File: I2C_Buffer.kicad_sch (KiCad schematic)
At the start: 6 parts, among them U2 LTC4300A-1IMS8_PBF

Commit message: BOM update
completed the BOM list
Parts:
- C19: MANUFACTURER (none) -> Murata Electronics; MANUFACTURER_PART_NUMBER (none) -> GCM155R71H103KA55J
- R11, R12, R3, R4: MANUFACTURER (none) -> Vishay; MANUFACTURER_PART_NUMBER (none) -> MCS0402MD1002BE100
- U2: MANUFACTURER (none) -> Analog Devices Inc.
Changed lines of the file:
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@@
+			)
+		)
+		(property "MANUFACTURER" "Vishay"
+			(at 175.006 76.962 0)
+			(effects
+				(font
+					(size 1.27 1.27)
+				)
+				(hide yes)
+			)
+		)
+		(property "MANUFACTURER_PART_NUMBER" "MCS0402MD1002BE100"
+			(at 175.006 76.962 0)
+			(effects
+				(font
+					(size 1.27 1.27)
+				)
+				(hide yes)
 			)
 		)
@@
 				)
 				(justify bottom)
+				(hide yes)
+			)
+		)
+		(property "MANUFACTURER" "Analog Devices Inc."
+			(at 133.35 78.74 0)
+			(effects
+				(font
+					(size 1.27 1.27)
+				)
 				(hide yes)
 			)
@@
 			)
 		)
+		(property "MANUFACTURER" "Vishay"
+			(at 120.65 76.708 0)
+			(effects
+				(font
+					(size 1.27 1.27)
+				)
+				(hide yes)
+			)
+		)
+		(property "MANUFACTURER_PART_NUMBER" "MCS0402MD1002BE100"
+			(at 120.65 76.708 0)
+			(effects
+				(font
+					(size 1.27 1.27)
+				)
+				(hide yes)
+			)
+		)
 		(pin "1"
 		)
@@
 			)
 		)
+		(property "MANUFACTURER" "Vishay"
+			(at 165.354 76.708 0)
+			(effects
+				(font
+					(size 1.27 1.27)
+				)
+				(hide yes)
+			)
+		)
+		(property "MANUFACTURER_PART_NUMBER" "MCS0402MD1002BE100"
+			(at 165.354 76.708 0)
+			(effects
+				(font
+					(size 1.27 1.27)
+				)
+				(hide yes)
+			)
+		)
 		(pin "1"
 		)
@@
 			)
 		)
+		(property "MANUFACTURER" "Vishay"
+			(at 128.778 76.454 0)
+			(effects
+				(font
+					(size 1.27 1.27)
+				)
+				(hide yes)
+			)
+		)
+		(property "MANUFACTURER_PART_NUMBER" "MCS0402MD1002BE100"
+			(at 128.778 76.454 0)
+			(effects
+				(font
+					(size 1.27 1.27)
+				)
+				(hide yes)
+			)
+		)
 		(pin "1"
 		)
@@
 			(effects
 				(font
+					(size 1.27 1.27)
+				)
+				(hide yes)
+			)
+		)
+		(property "MANUFACTURER" "Murata Electronics"
+			(at 131.572 66.802 90)
+			(effects
+				(font
+					(size 1.27 1.27)
+				)
+				(hide yes)
+			)
+		)
+		(property "MANUFACTURER_PART_NUMBER" "GCM155R71H103KA55J"
+			(at 131.572 66.802 90)
+			(effects
+				(font

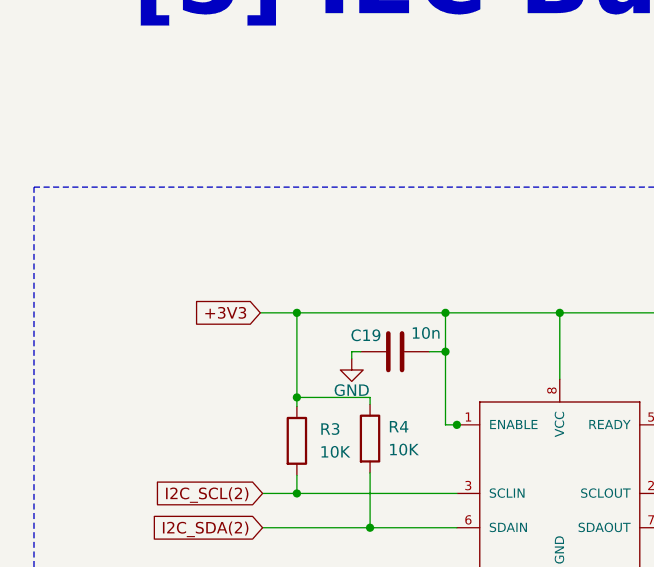
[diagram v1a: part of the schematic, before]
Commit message: Moved SD Card Slot
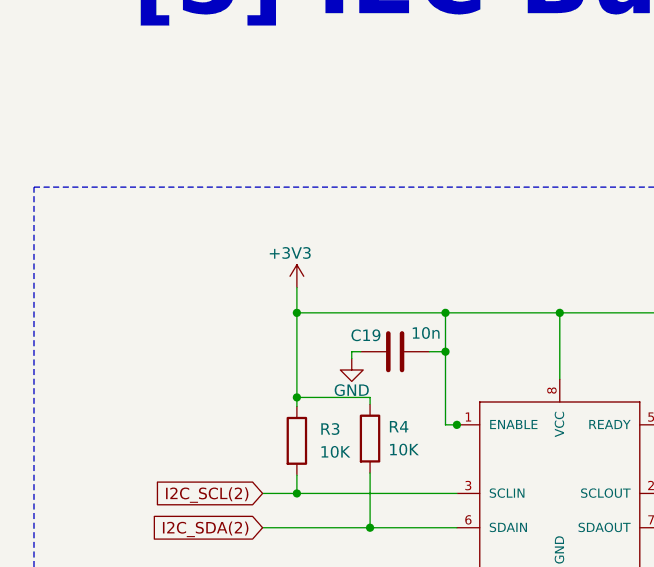
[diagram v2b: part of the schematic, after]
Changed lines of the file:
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@@
+	)
+	(junction
+		(at 120.65 62.484)
+		(diameter 0)
+		(color 0 0 0 0)
 	)
 	(junction
@@
 	)
 	(junction
-		(at 120.65 62.484)
-		(diameter 0)
-		(color 0 0 0 0)
-	)
-	(junction
 		(at 137.16 62.484)
 		(diameter 0)
@@
 	(wire
 		(pts
-			(xy 116.586 62.484) (xy 120.65 62.484)
-		)
-		(stroke
-			(width 0)
-			(type default)
-		)
-	)
-	(wire
-		(pts
 			(xy 126.746 67.564) (xy 126.746 66.802)
 		)
@@
 	(wire
 		(pts
+			(xy 120.65 59.69) (xy 120.65 62.484)
+		)
+		(stroke
+			(width 0)
+			(type default)
+		)
+	)
+	(wire
+		(pts
+			(xy 175.006 80.772) (xy 175.006 86.36)
+		)
+		(stroke
+			(width 0)
+			(type default)
+		)
+	)
+	(wire
+		(pts
+			(xy 165.354 80.518) (xy 165.354 82.55)
+		)
+		(stroke
+			(width 0)
+			(type default)
+		)
+	)
+	(wire
+		(pts
+			(xy 137.16 66.802) (xy 137.16 62.484)
+		)
+		(stroke
+			(width 0)
+			(type default)
+		)
+	)
+	(wire
+		(pts
+			(xy 116.84 82.55) (xy 120.65 82.55)
+		)
+		(stroke
+			(width 0)
+			(type default)
+		)
+	)
+	(wire
+		(pts
+			(xy 165.354 62.484) (xy 165.354 72.898)
+		)
+		(stroke
+			(width 0)
+			(type default)
+		)
+	)
+	(wire
+		(pts
+			(xy 135.382 66.802) (xy 137.16 66.802)
+		)
+		(stroke
+			(width 0)
+			(type default)
+		)
+	)
+	(wire
+		(pts
+			(xy 120.65 71.882) (xy 128.778 71.882)
+		)
+		(stroke
+			(width 0)
+			(type default)
+		)
+	)
+	(wire
+		(pts
+			(xy 149.86 62.484) (xy 149.86 69.85)
+		)
+		(stroke
+			(width 0)
+			(type default)
+		)
+	)
+	(wire
+		(pts
 			(xy 120.65 62.484) (xy 120.65 71.882)
 		)
@@
 	(wire
 		(pts
-			(xy 175.006 80.772) (xy 175.006 86.36)
-		)
-		(stroke
-			(width 0)
-			(type default)
-		)
-	)
-	(wire
-		(pts
-			(xy 165.354 80.518) (xy 165.354 82.55)
-		)
-		(stroke
-			(width 0)
-			(type default)
-		)
-	)
-	(wire
-		(pts
-			(xy 137.16 66.802) (xy 137.16 62.484)
-		)
-		(stroke
-			(width 0)
-			(type default)
-		)
-	)
-	(wire
-		(pts
-			(xy 116.84 82.55) (xy 120.65 82.55)
-		)
-		(stroke
-			(width 0)
-			(type default)
-		)
-	)
-	(wire
-		(pts
-			(xy 165.354 62.484) (xy 165.354 72.898)
-		)
-		(stroke
-			(width 0)
-			(type default)
-		)
-	)
-	(wire
-		(pts
-			(xy 135.382 66.802) (xy 137.16 66.802)
-		)
-		(stroke
-			(width 0)
-			(type default)
-		)
-	)
-	(wire
-		(pts
-			(xy 120.65 71.882) (xy 128.778 71.882)
-		)
-		(stroke
-			(width 0)
-			(type default)
-		)
-	)
-	(wire
-		(pts
-			(xy 149.86 62.484) (xy 149.86 69.85)
-		)
-		(stroke
-			(width 0)
-			(type default)
-		)
-	)
-	(wire
-		(pts
 			(xy 128.778 86.36) (xy 138.43 86.36)
 		)
@@
 			(width 0)
 			(type default)
-		)
-	)
-	(global_label "+3V3"
-		(shape input)
-		(at 116.586 62.484 180)
-		(fields_autoplaced yes)
-		(effects
-			(font
-				(size 1.27 1.27)
-			)
-			(justify right)
-		)
-		(property "Intersheetrefs" "${INTERSHEET_REFS}"
-			(at 108.5208 62.484 0)
-			(effects
-				(font
-					(size 1.27 1.27)
-				)
-				(justify right)
-				(hide yes)
-			)
 		)
 	)
@@
 			)
 		)
+	)
+	(symbol
+		(lib_id "power:+3V3")
+		(at 120.65 59.69 0)
+		(unit 1)
+		(exclude_from_sim no)
+		(in_bom yes)
+		(on_board yes)
+		(dnp no)
+		(property "Reference" "#PWR039"
+			(at 120.65 63.5 0)
+			(effects
+				(font
+					(size 1.27 1.27)
+				)
+				(hide yes)
+			)
+		)
+		(property "Value" "+3V3"
+			(at 119.888 55.88 0)
+			(effects
+				(font
+					(size 1.27 1.27)
+				)
+			)
+		)
+		(property "Footprint" ""
+			(at 120.65 59.69 0)
+			(effects
+				(font
+					(size 1.27 1.27)
+				)
+				(hide yes)
+			)
+		)
+		(property "Datasheet" ""
+			(at 120.65 59.69 0)
+			(effects
+				(font
+					(size 1.27 1.27)
+				)
+				(hide yes)
+			)
+		)
+		(property "Description" "Power symbol creates a global label with name \"+3V3\""
+			(at 120.65 59.69 0)
+			(effects
+				(font
+					(size 1.27 1.27)
+				)
+				(hide yes)
+			)
+		)
+		(pin "1"
+		)
+		(instances
+			(project "adapter-pcb"
+				(path "/94da9b83-1146-4f01-8e34-8153765b0257/8f9a2a35-dce8-46a6-bed9-0172c40628c2"
+					(reference "#PWR039")
+					(unit 1)
+				)
+			)
+		)

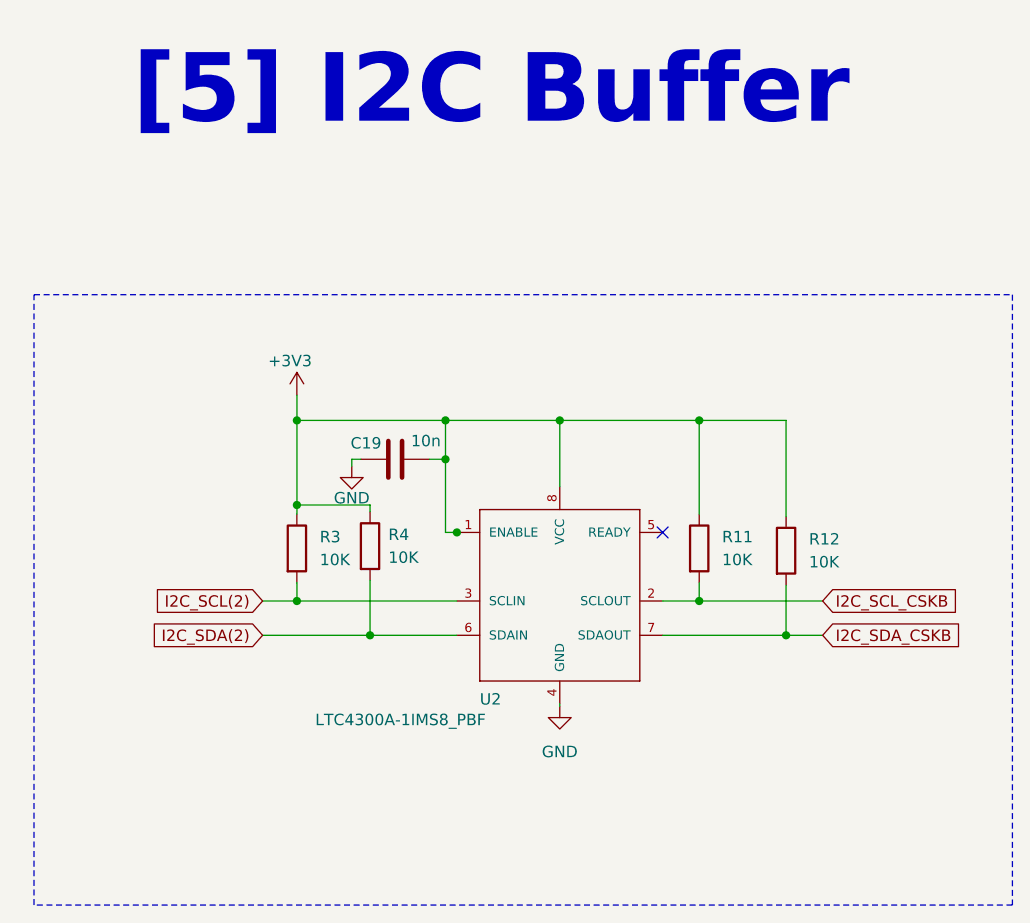
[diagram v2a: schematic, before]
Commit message: Added hierarchical lables to the schematic
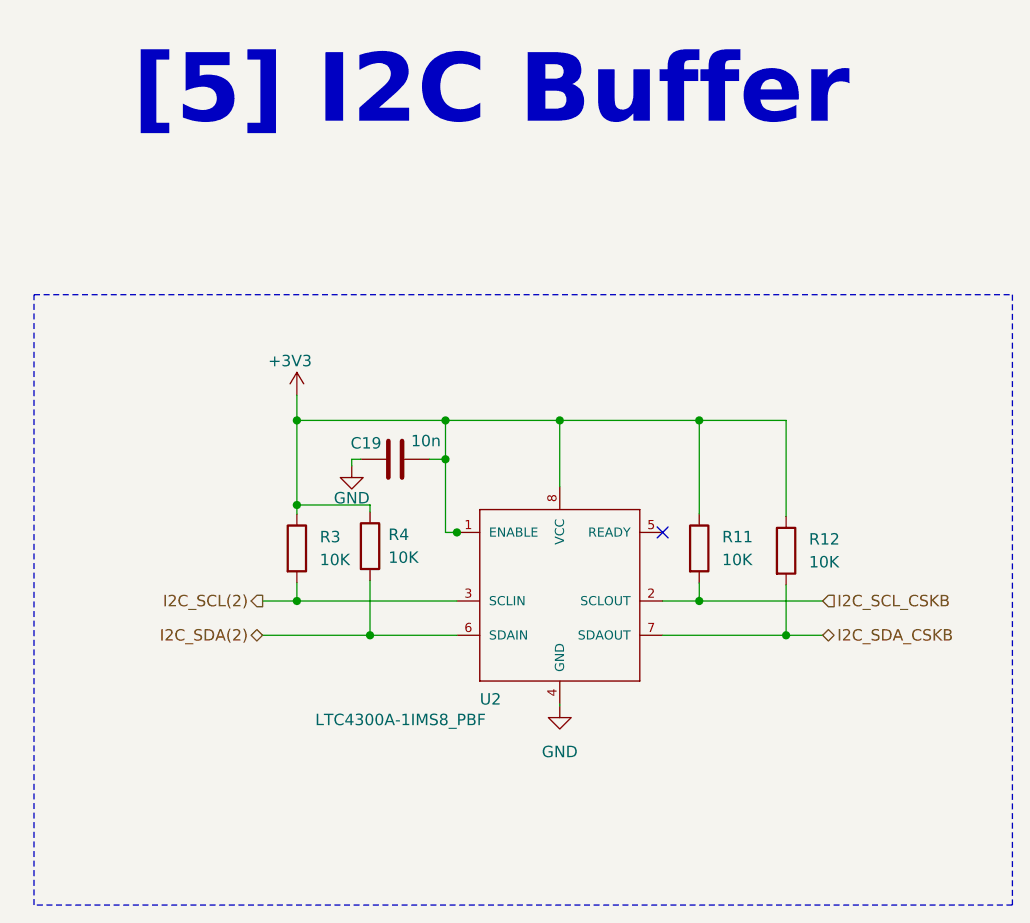
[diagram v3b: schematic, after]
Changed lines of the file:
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@@
 		)
 	)
-	(global_label "I2C_SDA(2)"
+	(hierarchical_label "I2C_SCL_CSKB"
 		(shape input)
-		(at 116.84 86.36 180)
-		(fields_autoplaced yes)
+		(at 179.07 82.55 0)
+		(effects
+			(font
+				(size 1.27 1.27)
+			)
+			(justify left)
+		)
+	)
+	(hierarchical_label "I2C_SDA_CSKB"
+		(shape bidirectional)
+		(at 179.07 86.36 0)
+		(effects
+			(font
+				(size 1.27 1.27)
+			)
+			(justify left)
+		)
+	)
+	(hierarchical_label "I2C_SCL(2)"
+		(shape output)
+		(at 116.84 82.55 180)
 		(effects
 			(font
@@
 			(justify right)
 		)
-		(property "Intersheetrefs" "${INTERSHEET_REFS}"
-			(at 103.3319 86.36 0)
-			(effects
-				(font
-					(size 1.27 1.27)
-				)
-				(justify right)
-				(hide yes)
-			)
-		)
 	)
-	(global_label "I2C_SCL(2)"
-		(shape input)
-		(at 116.84 82.55 180)
-		(fields_autoplaced yes)
+	(hierarchical_label "I2C_SDA(2)"
+		(shape bidirectional)
+		(at 116.84 86.36 180)
 		(effects
 			(font
@@
 			(justify right)
 		)
-		(property "Intersheetrefs" "${INTERSHEET_REFS}"
-			(at 103.3924 82.55 0)
-			(effects
-				(font
-					(size 1.27 1.27)
-				)
-				(justify right)
-				(hide yes)
-			)
-		)
 	)
-	(global_label "I2C_SDA_CSKB"
-		(shape input)
-		(at 179.07 86.36 0)
-		(fields_autoplaced yes)
-		(effects
-			(font
-				(size 1.27 1.27)
-			)
-			(justify left)
-		)
-		(property "Intersheetrefs" "${INTERSHEET_REFS}"
-			(at 195.6623 86.36 0)
-			(effects
-				(font
-					(size 1.27 1.27)
-				)
-				(justify left)
-				(hide yes)
-			)
-		)
-	)
-	(global_label "I2C_SCL_CSKB"
-		(shape input)
-		(at 179.07 82.55 0)
-		(fields_autoplaced yes)
-		(effects
-			(font
-				(size 1.27 1.27)
-			)
-			(justify left)
-		)
-		(property "Intersheetrefs" "${INTERSHEET_REFS}"
-			(at 195.6018 82.55 0)
-			(effects
-				(font
-					(size 1.27 1.27)
-				)
-				(justify left)
-				(hide yes)
-			)
-		)
-	)
